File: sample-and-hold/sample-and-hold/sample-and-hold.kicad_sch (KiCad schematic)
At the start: 36 parts, among them J1 Power Connector, J2 CLOCK_IN, J3 SIGNAL_IN, J4 SIGNAL_IN, Q1 J112, Q2 2N3904, U1 TL072, U2 TL072

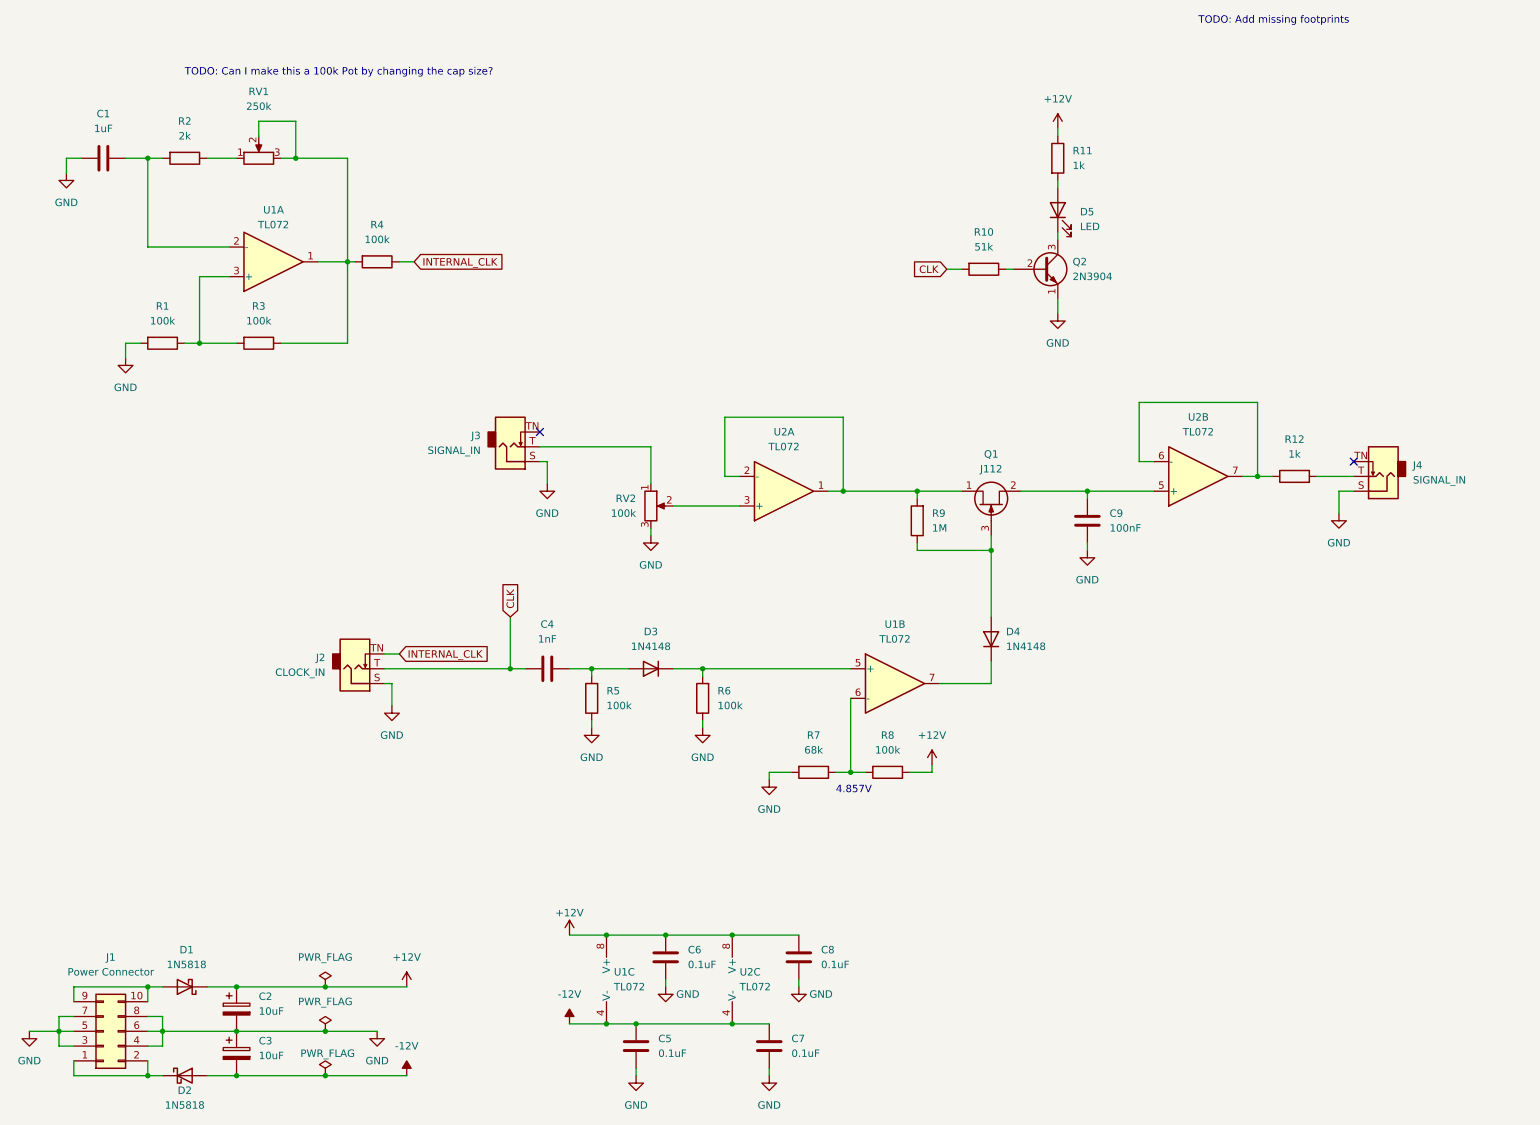
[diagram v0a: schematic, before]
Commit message: Added REV1 of sample and hold board/panel
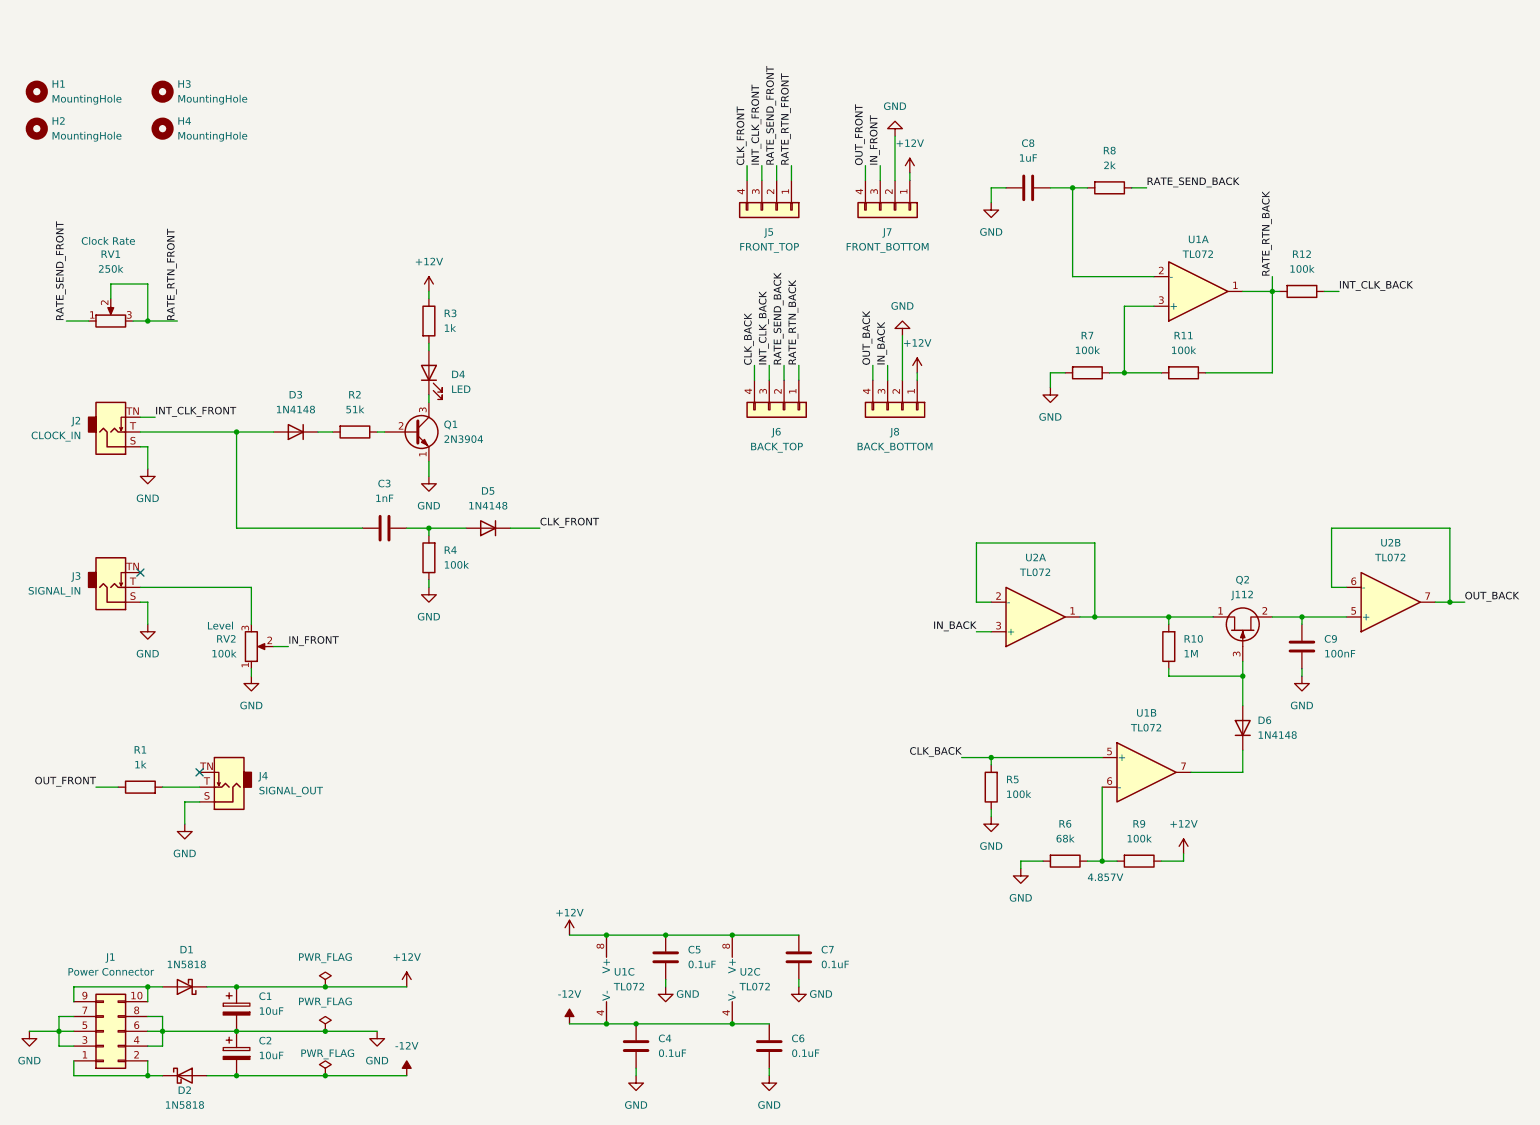
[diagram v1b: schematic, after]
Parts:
- removed C4: 1nF, Capacitor_THT:C_Rect_L7.2mm_W2.5mm_P5.00mm_FKS2_FKP2_MKS2_MKP2, symbol Device:C
- removed R12: 1k, Resistor_THT:R_Axial_DIN0207_L6.3mm_D2.5mm_P10.16mm_Horizontal, symbol Device:R
- removed R5: 100k, Resistor_THT:R_Axial_DIN0207_L6.3mm_D2.5mm_P10.16mm_Horizontal, symbol Device:R
- added C3: 1nF, Capacitor_THT:C_Rect_L7.2mm_W2.5mm_P5.00mm_FKS2_FKP2_MKS2_MKP2, symbol Device:C
- added D5: 1N4148, Diode_THT:D_DO-35_SOD27_P7.62mm_Horizontal, symbol Diode:1N4148
- added H1, H2, H3, H4: MountingHole, MountingHole:MountingHole_2.2mm_M2, symbol Mechanical:MountingHole
- added J5: FRONT_TOP, Connector_PinHeader_2.54mm:PinHeader_1x04_P2.54mm_Vertical, symbol Connector_Generic:Conn_01x04
- added J6: BACK_TOP, Connector_PinHeader_2.54mm:PinHeader_1x04_P2.54mm_Vertical, symbol Connector_Generic:Conn_01x04
- added J7: FRONT_BOTTOM, Connector_PinHeader_2.54mm:PinHeader_1x04_P2.54mm_Vertical, symbol Connector_Generic:Conn_01x04
- added J8: BACK_BOTTOM, Connector_PinHeader_2.54mm:PinHeader_1x04_P2.54mm_Vertical, symbol Connector_Generic:Conn_01x04
- added R1: 1k, Resistor_THT:R_Axial_DIN0207_L6.3mm_D2.5mm_P10.16mm_Horizontal, symbol Device:R
- added R4: 100k, Resistor_THT:R_Axial_DIN0207_L6.3mm_D2.5mm_P10.16mm_Horizontal, symbol Device:R
- J2, J3: footprint Tayda_Jacks:PJ-323M -> AudioJacks:Jack_3.5mm_QingPu_WQP-PJ398SM_Vertical; Manufacturer Part No. PJ-323M -> PJ-3001F; Supplier Part No. A-2557 -> A-2563
- J4: value SIGNAL_IN -> SIGNAL_OUT; footprint Tayda_Jacks:PJ-323M -> AudioJacks:Jack_3.5mm_QingPu_WQP-PJ398SM_Vertical; Manufacturer Part No. PJ-323M -> PJ-3001F; Supplier Part No. A-2557 -> A-2563
- RV1, RV2: footprint (none) -> Alpha_Pots:Potentiometer_Alpha_RV09AF-40-20K_Single_Vertical
- renumbered C2 to C1, C3 to C2, C5 to C4, C6 to C5, C7 to C6, C8 to C7, C1 to C8, D5 to D4, D4 to D6, Q2 to Q1, Q1 to Q2, R9 to R10, R3 to R11, R4 to R12, R10 to R2, R11 to R3, R6 to R5, R7 to R6, R1 to R7, R2 to R8, R8 to R9
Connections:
- net +12V: now also J7.1 (Pin_1), J8.1 (Pin_1)
- net GND: now also RV2.1, J7.2 (Pin_2), J8.2 (Pin_2), R4.1; no longer RV2.3
- net CLK_BACK: now reaches R5.2, U1.5 (+)
- net CLK_BACK: now also J6.4 (Pin_4); no longer D3.1 (K)
- net IN_BACK: now reaches U2.3 (+)
- net IN_BACK: now also J8.3 (Pin_3); no longer RV2.2
- net OUT_BACK: now reaches U2.6 (-), U2.7
- net OUT_BACK: now also J8.4 (Pin_4)
- net at J4.T: now also R1.2
- net RATE_RTN_BACK: now reaches R11.1, R12.2, U1.1
- net RATE_RTN_BACK: now also J6.1 (Pin_1); no longer RV1.2, RV1.3
- net at D3.2 (A): now also J2.T, C3.1
- net at J3.T: now also RV2.3; no longer RV2.1
- net RATE_SEND_BACK: now reaches R8.1
- net RATE_SEND_BACK: now also J6.2 (Pin_2); no longer RV1.1
- net CLK: no longer names the net of R2.2
- net CLK: now also D3.1 (K); no longer J2.T
- net INTERNAL_CLK renamed INT_CLK_BACK
- net INT_CLK_BACK: now also J6.3 (Pin_3); no longer J2.TN
- new net: C3.2, D5.2 (A), R4.2
- new net CLK_FRONT: D5.1 (K), J5.4 (Pin_4)
- new net INT_CLK_FRONT: J2.TN, J5.3 (Pin_3)
- new net IN_FRONT: J7.3 (Pin_3), RV2.2
- new net OUT_FRONT: J7.4 (Pin_4), R1.1
- new net RATE_RTN_FRONT: J5.1 (Pin_1), RV1.2, RV1.3
- new net RATE_SEND_FRONT: J5.2 (Pin_2), RV1.1
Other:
- note added: "Clock Rate"
- note added: "Level"
- note removed: "TODO: Add missing footprints"
- note removed: "TODO: Can I make this a 100k Pot by changing the cap size?"
- moved on the sheet: C8, C9, D4, D6, J2, J3, Q1, Q2, R10, R11, R12, R2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

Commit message: Simplified keyboard for rev1
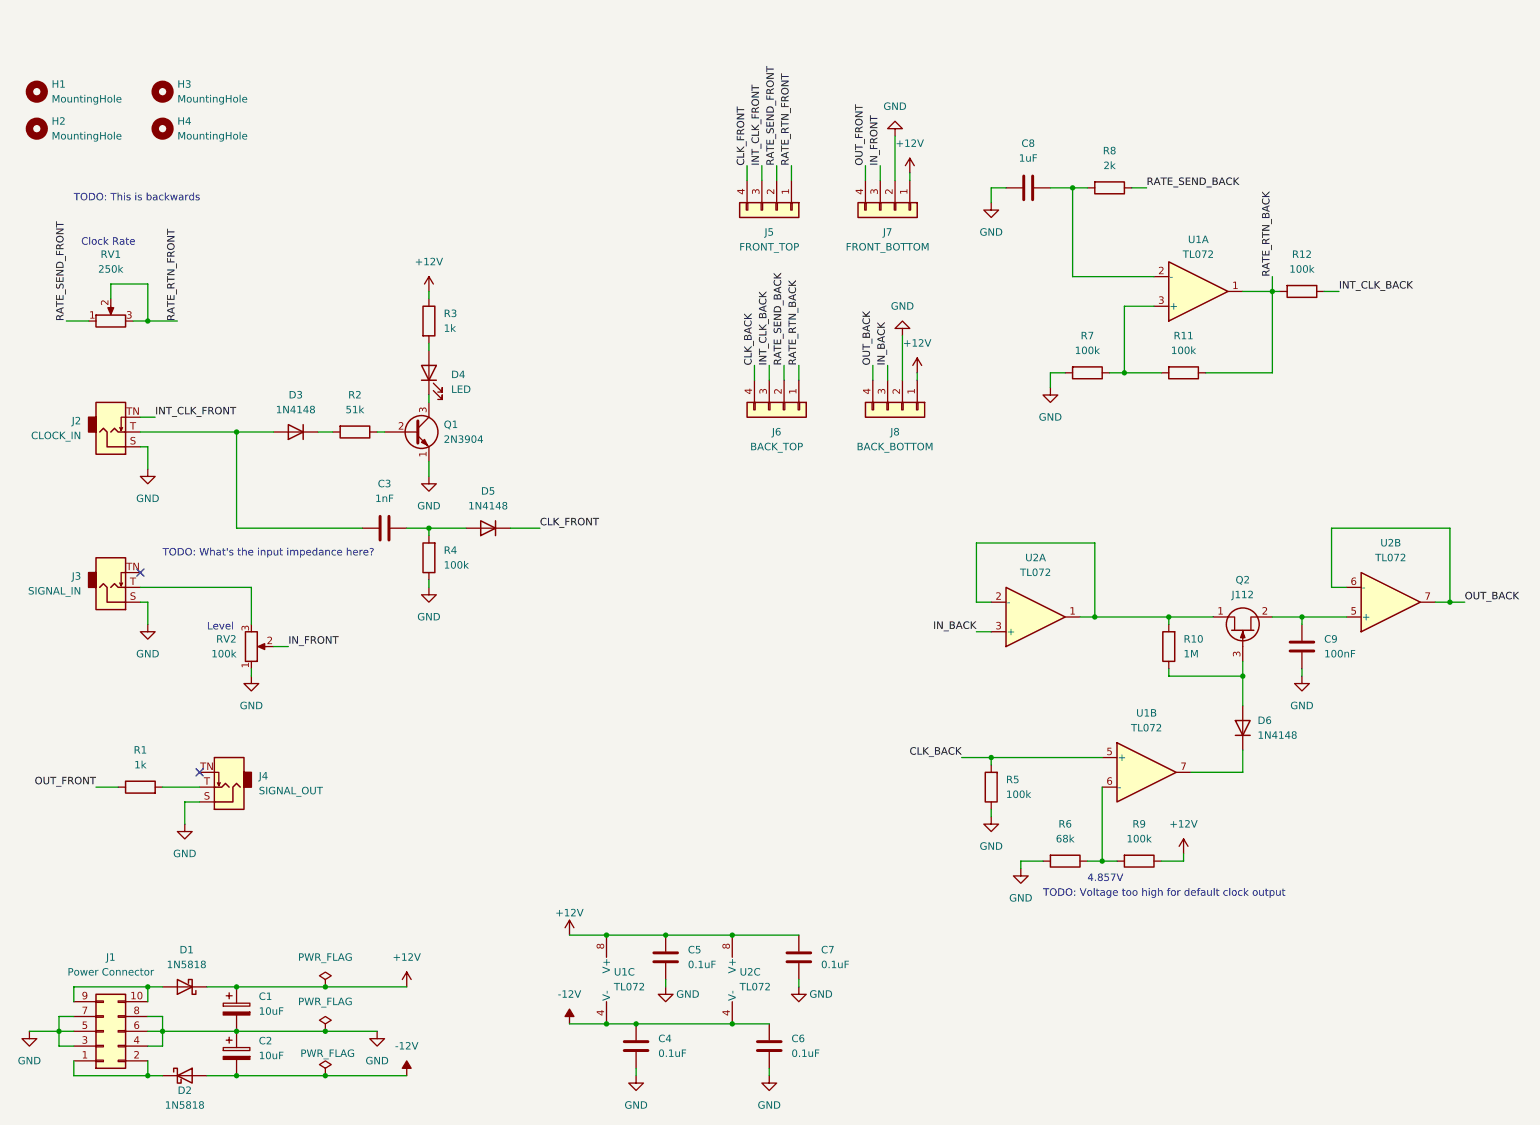
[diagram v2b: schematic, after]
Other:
- note added: "TODO: This is backwards"
- note added: "TODO: Voltage too high for default clock output"
- note added: "TODO: What's the input impedance here?"
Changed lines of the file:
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@@
+    (effects (font (size 1.27 1.27)) (justify left bottom))
+  )
+  (text "TODO: Voltage too high for default clock output" (at 196.85 157.48 0)
+    (effects (font (size 1.27 1.27)) (justify left bottom))
+  )
+  (text "TODO: This is backwards" (at 30.48 38.1 0)
     (effects (font (size 1.27 1.27)) (justify left bottom))
   )
@@
     (effects (font (size 1.27 1.27)) (justify left bottom))
   )
+  (text "TODO: What's the input impedance here?" (at 45.72 99.06 0)
+    (effects (font (size 1.27 1.27)) (justify left bottom))
+  )
